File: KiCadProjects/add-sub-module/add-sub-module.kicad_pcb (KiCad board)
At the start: 2 copper layers, 56 x 68 mm, 32 parts, among them J1 2x4_Header, J2 1x2_Header, M1 MountingHole_2.2mm_M2_Pad, M2 MountingHole_2.2mm_M2_Pad, M3 MountingHole_2.2mm_M2_Pad, M4 MountingHole_2.2mm_M2_Pad

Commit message: initial updates after meeting
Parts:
- MUX 2:1: renamed from MUX 2-1
- NAND 2inp: renamed from NAND 2CH
- NAND 3inp: renamed from NAND 3CH
- NOR 2inp: renamed from NOR 2CH
- NOT: renamed from NOT 1CH
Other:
- board text added: "+5V"
- board text added: "ADD/SUB"
- board text added: "CARRY IN"
- board text added: "CARRY OUT/ BORROW OUT"
- board text added: "CLK"
- board text added: "Full Adder/Subtractor Module"
- board text added: "GND"
- board text added: "RST"
- board text added: "SUM"
- board text added: "X/CA"
- board text added: "Y/KA"
- board text removed: "Adder-Subtractor Module"

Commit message: final updates for Revision A
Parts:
- removed M1, M2, M3, M4: MountingHole_2.2mm_M2_Pad, MountingHole:MountingHole_2.2mm_M2_Pad
- added H1: MountingHole_Pad, MountingHole:MountingHole_3.2mm_M3_DIN965_Pad, F.Cu at (100.2, 67.0)
- added H2: MountingHole_Pad, MountingHole:MountingHole_3.2mm_M3_DIN965_Pad, F.Cu at (145.2, 67.0)
- added H3: MountingHole_Pad, MountingHole:MountingHole_3.2mm_M3_DIN965_Pad, F.Cu at (100.2, 121.0)
- added H4: MountingHole_Pad, MountingHole:MountingHole_3.2mm_M3_DIN965_Pad, F.Cu at (145.2, 121.0)
- added J3: Conn_01x02_Pin, Connector_PinHeader_2.54mm:PinHeader_1x02_P2.54mm_Vertical, B.Cu at (147.2, 92.7)
- C1, C2, C3, C4, C5: footprint Capacitor_THT:C_Disc_D4.7mm_W2.5mm_P5.00mm -> Capacitor_THT:C_Disc_D5.0mm_W2.5mm_P5.00mm
- J1: value 2x4_Header -> Conn_01x04_Pin; footprint Connector_PinHeader_2.54mm:PinHeader_2x04_P2.54mm_Vertical -> Connector_PinHeader_2.54mm:PinHeader_1x04_P2.54mm_Vertical
- J2: value 1x2_Header -> Conn_01x04_Pin; footprint Connector_PinHeader_2.54mm:PinHeader_1x02_P2.54mm_Vertical -> Connector_PinHeader_2.54mm:PinHeader_1x04_P2.54mm_Vertical
- R1, R2, R3, R4, R5, R6: value 1k -> 330
- U1: renamed from NAND 3inp
- U2: renamed from NAND 2inp
- U3: renamed from NOR 2inp
- U4: renamed from MUX 2:1
- moved J2 54.1 mm to (98.2, 77.5)
- moved G*** 30.6 mm to (146.0, 76.0)
- moved C5 25.0 mm to (127.0, 105.5), turned to -90 degrees
- moved C4 24.4 mm to (127.0, 101.5), turned to 90 degrees
- moved C2 21.5 mm to (127.0, 81.5), turned to 90 degrees
- moved C3 21.2 mm to (127.0, 85.5), turned to -90 degrees
- moved C1 20.2 mm to (127.0, 65.5), turned to -90 degrees
- moved R4 17.8 mm to (105.1, 95.8), turned to 180 degrees
- moved R3 14.4 mm to (105.1, 92.2), turned to 180 degrees
- moved J1 13.9 mm to (98.2, 103.0)
- moved D4 11.0 mm to (109.2, 106.5)
- moved D1 8.95 mm to (109.2, 98.0)
- moved REF** 7.60 mm to (108.5, 74.2)
- moved D3 7.58 mm to (109.2, 82.0)
- moved R6 6.52 mm to (141.5, 105.5), turned to -90 degrees
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- renumbered NOT to U5
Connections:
- J1 pad 1: KA -> +5V
- J1 pad 2: +5V -> CLK
- J1 pad 3: CA -> RST
- J1 pad 4: RST -> GND
- J2 pad 1: SUM -> KA
- J2 pad 2: COUT -> CA
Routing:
- net +5V: track 135.0 -> 119.2 mm, vias 1 -> 0
- net KA: track 34.7 -> 45.2 mm, vias 1 -> 0
- net Net-(U1-1Y): track 18.3 -> 12.3 mm
- net Net-(U1-2B): track 79.1 -> 85.2 mm, vias 1 -> 0
- net GND: track 0.00 -> 6.00 mm
- net Net-(U1-1A): track 53.1 -> 59.0 mm
- net Net-(D4-K): track 6.88 -> 12.5 mm
- net ADD/SUB: track 52.7 -> 47.3 mm
- net Net-(D3-K): track 6.67 -> 12.0 mm
- net Net-(U3-1Y): track 49.1 -> 44.9 mm
- net Net-(U3-2B): track 39.5 -> 35.8 mm
- net CARRY: track 45.5 -> 49.1 mm
- net Net-(U1-2A): track 56.7 -> 53.1 mm, vias 0 -> 1
- net Net-(D6-K): track 9.05 -> 6.14 mm
- net Net-(U1-3Y): track 37.4 -> 34.5 mm
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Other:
- board size 56 x 68 mm -> 54 x 63 mm
- board text added: "CARRY OUT / BORROW OUT"
- board text added: "COUT"
- board text added: "MUX 2:1"
- board text added: "NAND 2inp"
- board text added: "NAND 3inp"
- board text added: "NOR 2inp"
- board text added: "NOT"
- board text removed: "CARRY OUT/ BORROW OUT"

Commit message: FINAL FINAL final updates for Rev. A
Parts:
- U1: value CD74HCT10E -> IC-14P
- U2: value SN74HCT00N -> IC-14P
- U3: value SN74HCT02N -> IC-14P
- U4: value SN74HCT257N -> IC-16P
- U5: value CD74HCT04E -> IC-14P
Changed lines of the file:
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@@
 			)
 		)
-		(property "Value" "SN74HCT257N"
+		(property "Value" "IC-16P"
 			(at 3.81 20.11 0)
 			(layer "F.Fab")
@@
 			)
 		)
-		(property "Datasheet" "SN74HCT257N"
+		(property "Datasheet" ""
 			(at 0 0 0)
 			(unlocked yes)
@@
 			)
 		)
-		(property "Description" ""
+		(property "Description" "SN74HCT257N"
 			(at 0 0 0)
 			(unlocked yes)
@@
 			)
 		)
-		(property "Value" "CD74HCT10E"
+		(property "Value" "IC-14P"
 			(at 3.81 17.57 0)
 			(layer "F.Fab")
@@
 			)
 		)
-		(property "Datasheet" "CD74HCT10E"
+		(property "Datasheet" ""
 			(at 0 0 0)
 			(unlocked yes)
@@
 			)
 		)
-		(property "Description" ""
+		(property "Description" "CD74HCT10E"
 			(at 0 0 0)
 			(unlocked yes)
@@
 			)
 		)
-		(property "Value" "SN74HCT00N"
+		(property "Value" "IC-14P"
 			(at 3.81 17.57 0)
 			(layer "F.Fab")
@@
 			)
 		)
-		(property "Datasheet" "SN74HCT00N"
+		(property "Datasheet" ""
 			(at 0 0 0)
 			(unlocked yes)
@@
 			)
 		)
-		(property "Description" ""
+		(property "Description" "SN74HCT00N"
 			(at 0 0 0)
 			(unlocked yes)
@@
 			)
 		)
-		(property "Value" "SN74HCT02N"
+		(property "Value" "IC-14P"
 			(at 3.81 17.57 0)
 			(layer "F.Fab")
@@
 			)
 		)
-		(property "Datasheet" "SN74HCT02N"
+		(property "Datasheet" ""
 			(at 0 0 0)
 			(unlocked yes)
@@
 			)
 		)
-		(property "Description" ""
+		(property "Description" "SN74HCT02N"
 			(at 0 0 0)
 			(unlocked yes)
@@
 			)
 		)
-		(property "Value" "CD74HCT04E"
+		(property "Value" "IC-14P"
 			(at 3.81 17.57 0)
 			(layer "F.Fab")
@@
 			)
 		)
-		(property "Datasheet" "CD74HCT04E"
+		(property "Datasheet" ""
 			(at 0 0 0)
 			(unlocked yes)
@@
 			)
 		)
-		(property "Description" ""
+		(property "Description" "CD74HCT04E"
 			(at 0 0 0)
 			(unlocked yes)

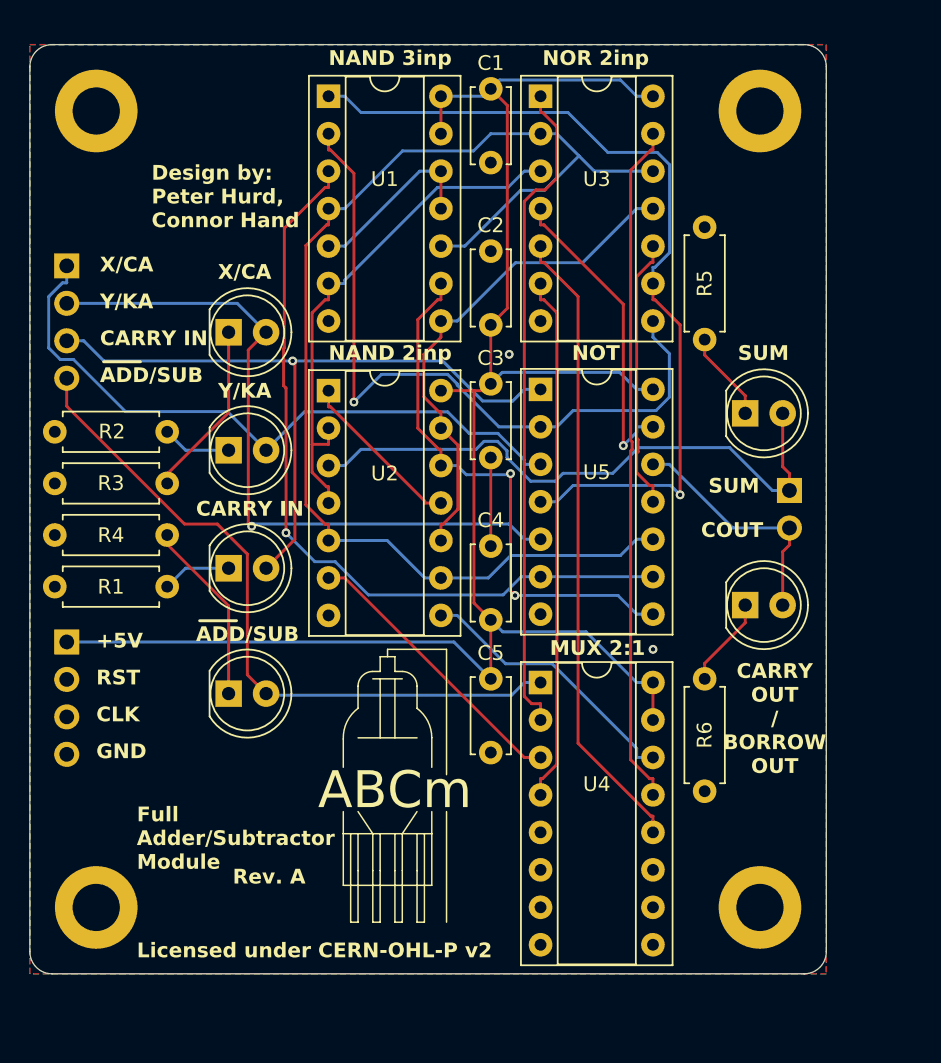
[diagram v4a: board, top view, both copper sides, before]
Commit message: Small changes to PCB, grounded MUX OE pin and updated PCB from schematic
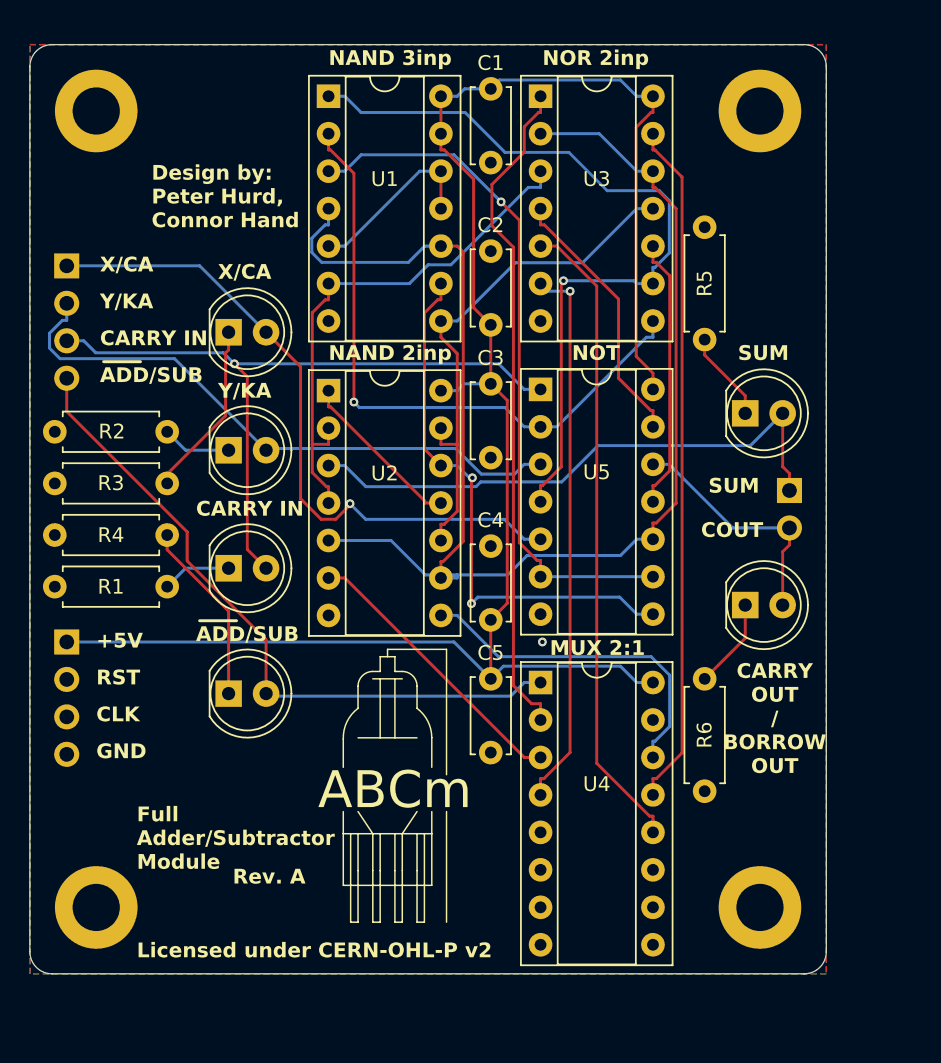
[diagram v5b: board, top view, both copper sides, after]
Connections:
- J2 pad 1: KA -> CA
- J2 pad 2: CA -> KA
- U4 pad 15: +5V -> GND
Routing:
- net Net-(U1-2B): track 85.2 -> 98.0 mm
- net GND: track 6.00 -> 0.00 mm, vias 2 -> 1
- net Net-(U1-1B): track 49.1 -> 43.6 mm
- net Net-(U1-2A): track 53.1 -> 47.8 mm
- net Net-(U1-1A): track 59.0 -> 54.1 mm
- net Net-(U2-3Y): track 18.7 -> 23.3 mm
- net KA: track 45.2 -> 40.9 mm
- net +5V: track 119.2 -> 123.3 mm
- net Net-(U3-2Y): track 21.3 -> 18.2 mm, vias 1 -> 0
- net CA: track 48.2 -> 46.0 mm
- net SUM: track 40.9 -> 38.9 mm
- net Net-(U3-2B): track 35.8 -> 37.3 mm, vias 0 -> 1
- net ADD/SUB: track 47.3 -> 46.0 mm
- net Net-(U1-3Y): track 34.5 -> 35.7 mm
- net CARRY: track 49.1 -> 48.2 mm
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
